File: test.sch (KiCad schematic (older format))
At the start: 6 parts, among them J1 Conn_01x32_Female, J2 Conn_01x32_Female, J3 DB9_Male, J4 Conn_01x32_Female, J5 Conn_01x32_Female, U1 MCP2551-I-SN

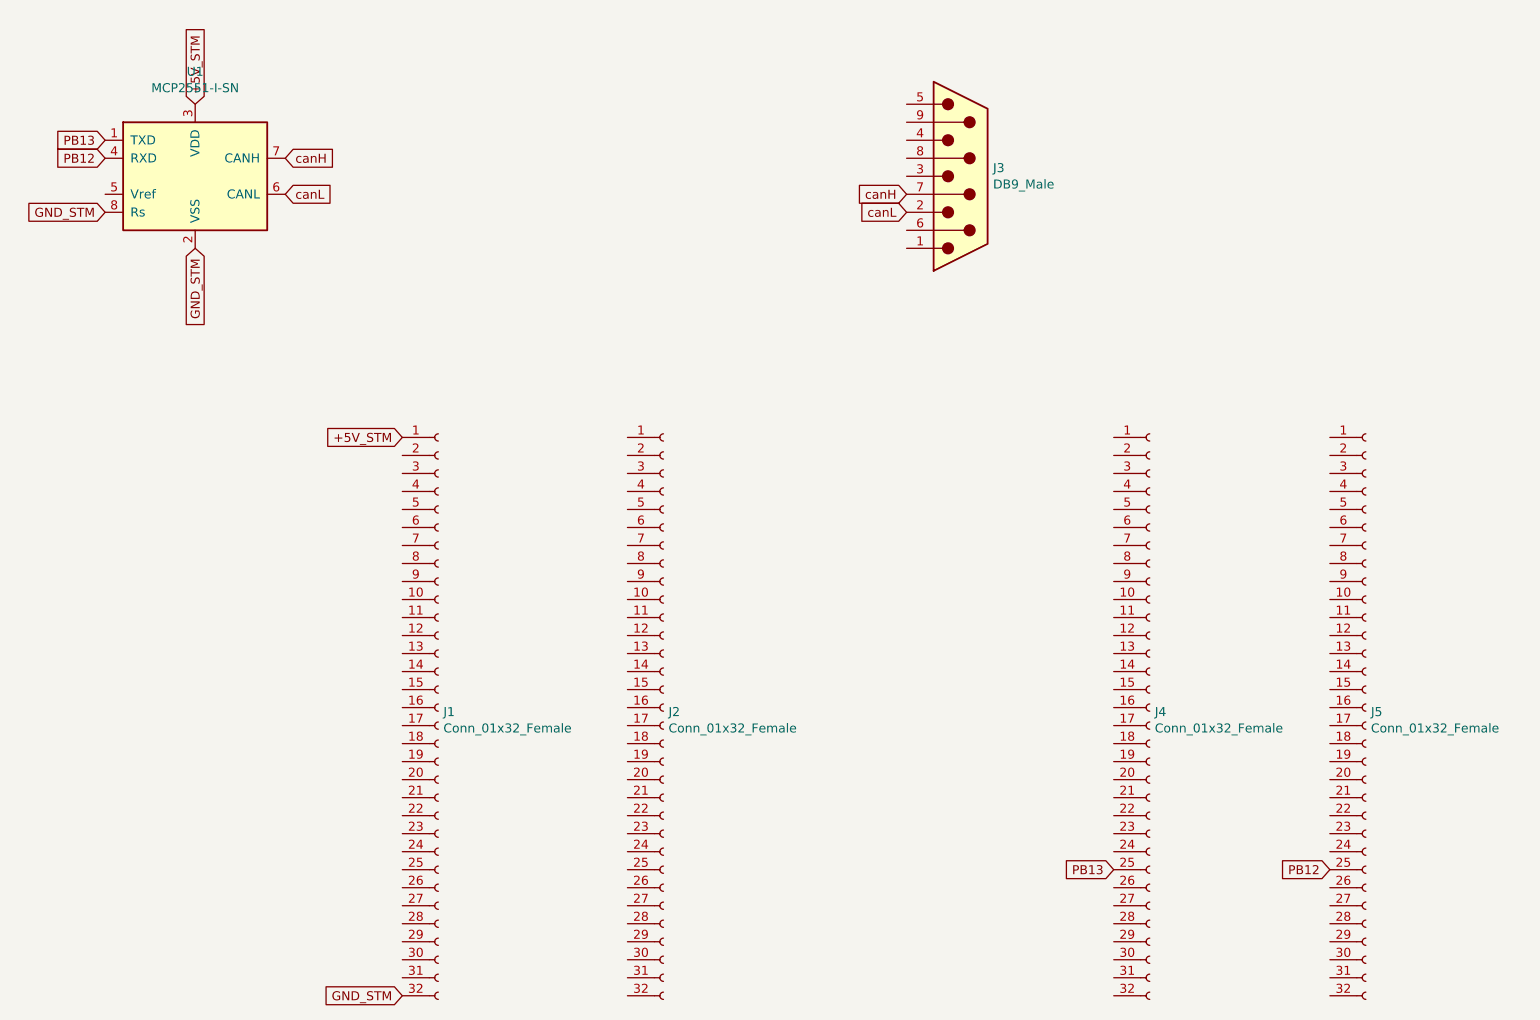
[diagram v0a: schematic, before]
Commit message: use less pin sockets
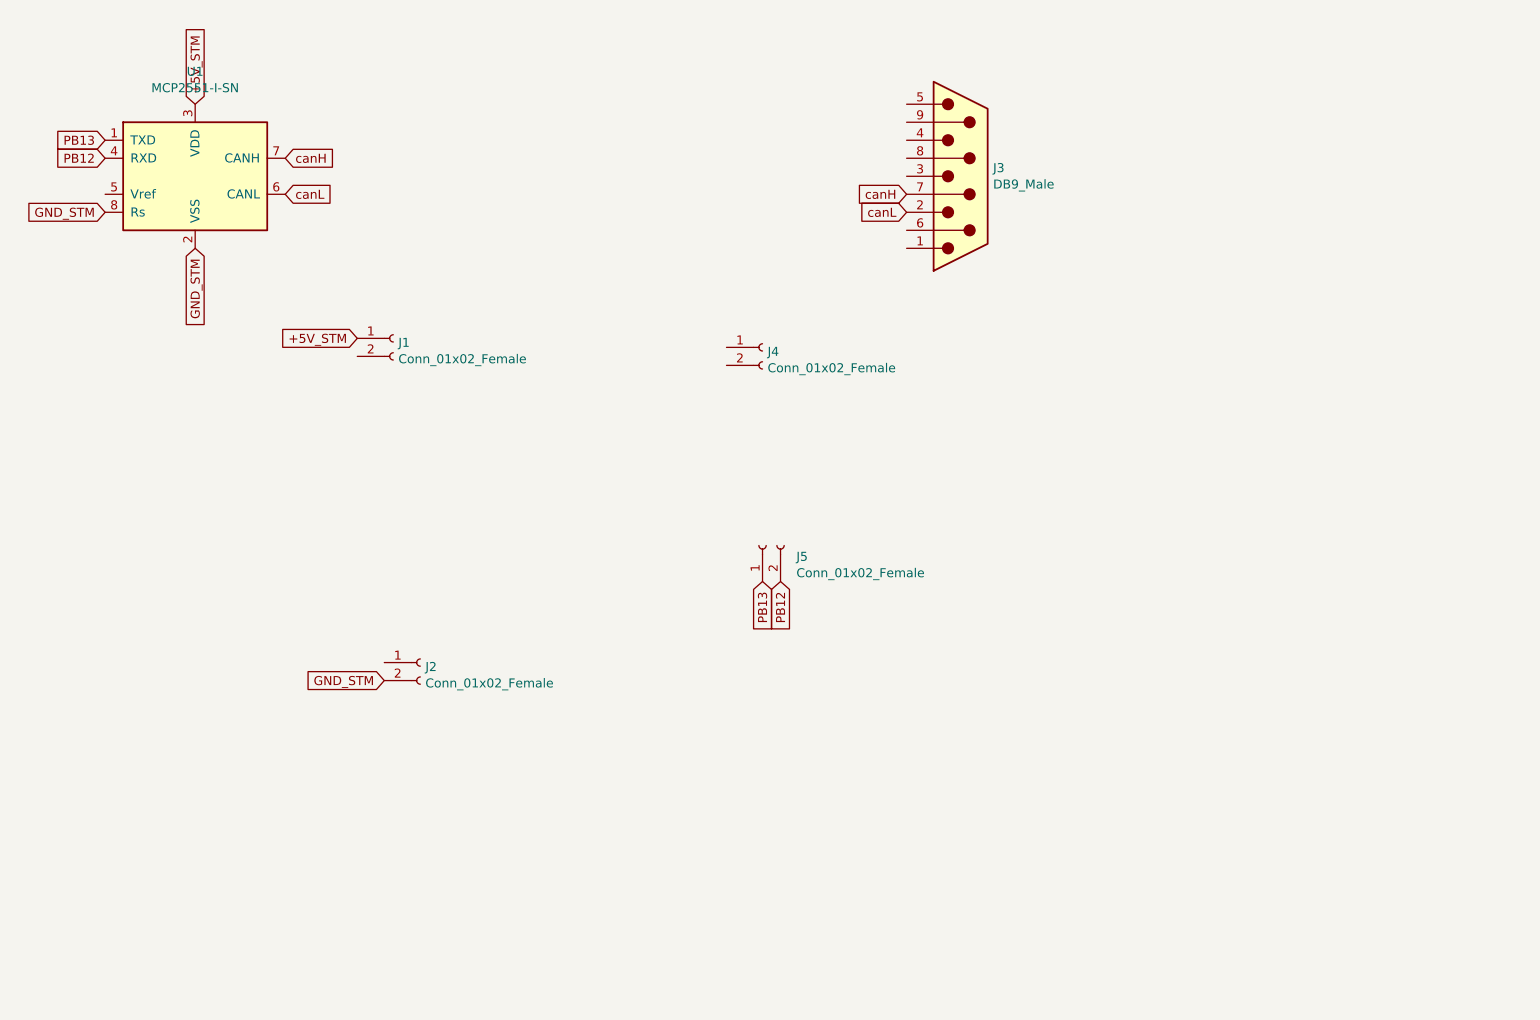
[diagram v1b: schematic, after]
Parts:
- removed J1, J2, J4, J5: Conn_01x32_Female, Connector_PinSocket_2.54mm:PinSocket_1x32_P2.54mm_Vertical, symbol Connector:Conn_01x32_Female
- added J1, J2, J4, J5: Conn_01x02_Female, Connector_PinSocket_2.54mm:PinSocket_1x02_P2.54mm_Vertical, symbol Connector:Conn_01x02_Female
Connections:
- net +5V_STM: now also J1.1 (Pin_1)
- net GND_STM: now also J2.2 (Pin_2)
- net PB12: now also J5.2 (Pin_2)
- net PB13: now also J5.1 (Pin_1)
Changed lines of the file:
@@
 Comment4 ""
 $EndDescr
-$Comp
-L Connector:Conn_01x32_Female J1
-U 1 1 5E3AAD21
-P 2950 4300
-F 0 "J1" H 2978 4276 50  0000 L CNN
-F 1 "Conn_01x32_Female" H 2978 4185 50  0000 L CNN
-F 2 "Connector_PinSocket_2.54mm:PinSocket_1x32_P2.54mm_Vertical" H 2950 4300 50  0001 C CNN
-F 3 "~" H 2950 4300 50  0001 C CNN
-	1    2950 4300
-	1    0    0    -1
-$EndComp
-$Comp
-L Connector:Conn_01x32_Female J2
-U 1 1 5E3AF919
-P 4200 4300
-F 0 "J2" H 4228 4276 50  0000 L CNN
-F 1 "Conn_01x32_Female" H 4228 4185 50  0000 L CNN
-F 2 "Connector_PinSocket_2.54mm:PinSocket_1x32_P2.54mm_Vertical" H 4200 4300 50  0001 C CNN
-F 3 "~" H 4200 4300 50  0001 C CNN
-	1    4200 4300
-	1    0    0    -1
-$EndComp
-$Comp
-L Connector:Conn_01x32_Female J4
-U 1 1 5E3B341A
-P 6900 4300
-F 0 "J4" H 6928 4276 50  0000 L CNN
-F 1 "Conn_01x32_Female" H 6928 4185 50  0000 L CNN
-F 2 "Connector_PinSocket_2.54mm:PinSocket_1x32_P2.54mm_Vertical" H 6900 4300 50  0001 C CNN
-F 3 "~" H 6900 4300 50  0001 C CNN
-	1    6900 4300
-	1    0    0    -1
-$EndComp
-$Comp
-L Connector:Conn_01x32_Female J5
-U 1 1 5E3B7068
-P 8100 4300
-F 0 "J5" H 8128 4276 50  0000 L CNN
-F 1 "Conn_01x32_Female" H 8128 4185 50  0000 L CNN
-F 2 "Connector_PinSocket_2.54mm:PinSocket_1x32_P2.54mm_Vertical" H 8100 4300 50  0001 C CNN
-F 3 "~" H 8100 4300 50  0001 C CNN
-	1    8100 4300
-	1    0    0    -1
-$EndComp
-Text GLabel 6700 5200 0    50   Input ~ 0
-PB13
-Text GLabel 7900 5200 0    50   Input ~ 0
+Text GLabel 4850 3600 3    50   Input ~ 0
 PB12
-Text GLabel 2750 2800 0    50   Input ~ 0
-+5V_STM
-Text GLabel 2750 5900 0    50   Input ~ 0
-GND_STM
 Text GLabel 1600 950  1    50   Input ~ 0
 +5V_STM
@@
 	1    0    0    -1
 $EndComp
+$Comp
+L Connector:Conn_01x02_Female J1
+U 1 1 5E4756EE
+P 2700 2250
+F 0 "J1" H 2728 2226 50  0000 L CNN
+F 1 "Conn_01x02_Female" H 2728 2135 50  0000 L CNN
+F 2 "Connector_PinSocket_2.54mm:PinSocket_1x02_P2.54mm_Vertical" H 2700 2250 50  0001 C CNN
+F 3 "~" H 2700 2250 50  0001 C CNN
+	1    2700 2250
+	1    0    0    -1
+$EndComp
+$Comp
+L Connector:Conn_01x02_Female J4
+U 1 1 5E48015E
+P 4750 2300
+F 0 "J4" H 4778 2276 50  0000 L CNN
+F 1 "Conn_01x02_Female" H 4778 2185 50  0000 L CNN
+F 2 "Connector_PinSocket_2.54mm:PinSocket_1x02_P2.54mm_Vertical" H 4750 2300 50  0001 C CNN
+F 3 "~" H 4750 2300 50  0001 C CNN
+	1    4750 2300
+	1    0    0    -1
+$EndComp
+$Comp
+L Connector:Conn_01x02_Female J2
+U 1 1 5E483C82
+P 2850 4050
+F 0 "J2" H 2878 4026 50  0000 L CNN
+F 1 "Conn_01x02_Female" H 2878 3935 50  0000 L CNN
+F 2 "Connector_PinSocket_2.54mm:PinSocket_1x02_P2.54mm_Vertical" H 2850 4050 50  0001 C CNN
+F 3 "~" H 2850 4050 50  0001 C CNN
+	1    2850 4050
+	1    0    0    -1
+$EndComp
+$Comp
+L Connector:Conn_01x02_Female J5
+U 1 1 5E48A586
+P 4750 3400
+F 0 "J5" V 4688 3212 50  0000 R CNN
+F 1 "Conn_01x02_Female" V 4597 3212 50  0000 R CNN
+F 2 "Connector_PinSocket_2.54mm:PinSocket_1x02_P2.54mm_Vertical" H 4750 3400 50  0001 C CNN
+F 3 "~" H 4750 3400 50  0001 C CNN
+	1    4750 3400
+	0    -1   -1   0
+$EndComp
+Text GLabel 2500 2250 0    50   Input ~ 0
++5V_STM
+Text GLabel 2650 4150 0    50   Input ~ 0
+GND_STM
+Text GLabel 4750 3600 3    50   Input ~ 0
+PB13
 $EndSCHEMATC

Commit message: Gerbers and BOM files
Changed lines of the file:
@@
 P 1600 1350
 F 0 "U1" H 1600 1931 50  0000 C CNN
-F 1 "MCP2551-I-SN" H 1600 1840 50  0000 C CNN
+F 1 "MCP2551-I-SN" H 1600 1350 50  0000 C CNN
 F 2 "Package_SO:SOIC-8_3.9x4.9mm_P1.27mm" H 1600 850 50  0001 C CIN
 F 3 "http://ww1.microchip.com/downloads/en/devicedoc/21667d.pdf" H 1600 1350 50  0001 C CNN

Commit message: housed db9
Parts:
- J3: footprint Connector_Dsub:DSUB-9_Male_Horizontal_P2.77x2.54mm_EdgePinOffset9.40mm -> Connector_Dsub:DSUB-9_Male_Horizontal_P2.77x2.84mm_EdgePinOffset4.94mm_Housed_MountingHolesOffset7.48mm
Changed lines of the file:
@@
 Text GLabel 2100 1450 2    50   Input ~ 0
 canL
-$Comp
-L Connector:DB9_Male J3
-U 1 1 5E492897
-P 5850 1350
-F 0 "J3" H 6030 1396 50  0000 L CNN
-F 1 "DB9_Male" H 6030 1305 50  0000 L CNN
-F 2 "Connector_Dsub:DSUB-9_Male_Horizontal_P2.77x2.54mm_EdgePinOffset9.40mm" H 5850 1350 50  0001 C CNN
-F 3 " ~" H 5850 1350 50  0001 C CNN
-	1    5850 1350
-	1    0    0    -1
-$EndComp
 Text GLabel 5550 1450 0    50   Input ~ 0
 canH
@@
 Text GLabel 4750 3600 3    50   Input ~ 0
 PB13
+$Comp
+L Connector:DB9_Male J3
+U 1 1 5E492897
+P 5850 1350
+F 0 "J3" H 6030 1396 50  0000 L CNN
+F 1 "DB9_Male" H 6030 1305 50  0000 L CNN
+F 2 "Connector_Dsub:DSUB-9_Male_Horizontal_P2.77x2.84mm_EdgePinOffset4.94mm_Housed_MountingHolesOffset7.48mm" H 5850 1350 50  0001 C CNN
+F 3 " ~" H 5850 1350 50  0001 C CNN
+	1    5850 1350
+	1    0    0    -1
+$EndComp
 $EndSCHEMATC

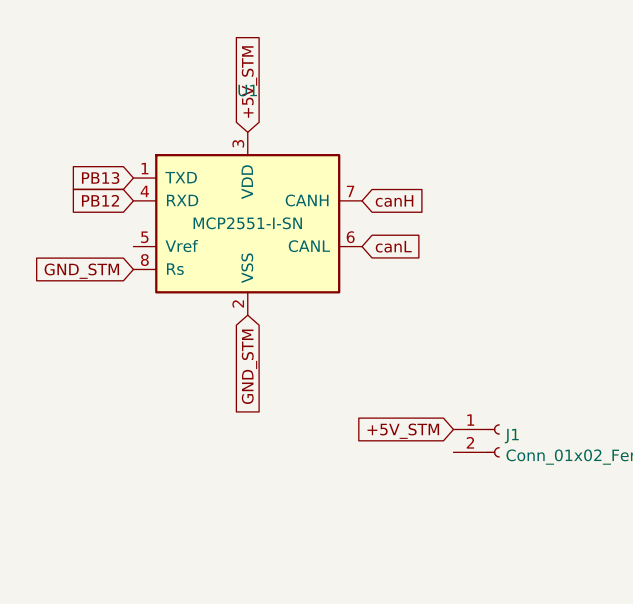
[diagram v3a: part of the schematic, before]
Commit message: regular mcp2551
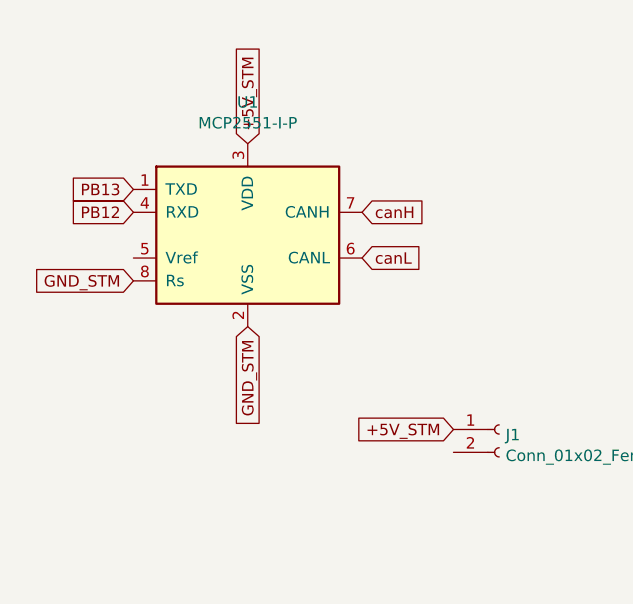
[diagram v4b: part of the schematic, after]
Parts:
- removed U1: MCP2551-I-SN, Package_SO:SOIC-8_3.9x4.9mm_P1.27mm, symbol Interface_CAN_LIN:MCP2551-I-SN
- added U1: MCP2551-I-P, Package_DIP:DIP-8_W7.62mm, symbol Interface_CAN_LIN:MCP2551-I-P
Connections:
- net +5V_STM: now also U1.3 (VDD)
- net GND_STM: now also U1.2 (VSS), U1.8 (Rs)
- net PB12: now also U1.4 (RXD)
- net PB13: now also U1.1 (TXD)
- net canH: now also U1.7 (CANH)
- net canL: now also U1.6 (CANL)
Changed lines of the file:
@@
 Text GLabel 4850 3600 3    50   Input ~ 0
 PB12
-Text GLabel 1600 950  1    50   Input ~ 0
+Text GLabel 1600 1000 1    50   Input ~ 0
 +5V_STM
-Text GLabel 1100 1250 0    50   Input ~ 0
+Text GLabel 1100 1300 0    50   Input ~ 0
 PB12
-Text GLabel 1100 1150 0    50   Input ~ 0
+Text GLabel 1100 1200 0    50   Input ~ 0
 PB13
-Text GLabel 1600 1750 3    50   Input ~ 0
+Text GLabel 1600 1800 3    50   Input ~ 0
 GND_STM
-Text GLabel 1100 1550 0    50   Input ~ 0
+Text GLabel 1100 1600 0    50   Input ~ 0
 GND_STM
-Text GLabel 2100 1250 2    50   Input ~ 0
+Text GLabel 2100 1300 2    50   Input ~ 0
 canH
-Text GLabel 2100 1450 2    50   Input ~ 0
+Text GLabel 2100 1500 2    50   Input ~ 0
 canL
 Text GLabel 5550 1450 0    50   Input ~ 0
@@
 Text GLabel 5550 1550 0    50   Input ~ 0
 canL
-$Comp
-L Interface_CAN_LIN:MCP2551-I-SN U1
-U 1 1 5E4B67C7
-P 1600 1350
-F 0 "U1" H 1600 1931 50  0000 C CNN
-F 1 "MCP2551-I-SN" H 1600 1350 50  0000 C CNN
-F 2 "Package_SO:SOIC-8_3.9x4.9mm_P1.27mm" H 1600 850 50  0001 C CIN
-F 3 "http://ww1.microchip.com/downloads/en/devicedoc/21667d.pdf" H 1600 1350 50  0001 C CNN
-	1    1600 1350
-	1    0    0    -1
-$EndComp
 $Comp
 L Connector:Conn_01x02_Female J1
@@
 	1    0    0    -1
 $EndComp
+$Comp
+L Interface_CAN_LIN:MCP2551-I-P U1
+U 1 1 5E503F33
+P 1600 1400
+F 0 "U1" H 1600 1981 50  0000 C CNN
+F 1 "MCP2551-I-P" H 1600 1890 50  0000 C CNN
+F 2 "Package_DIP:DIP-8_W7.62mm" H 1600 900 50  0001 C CIN
+F 3 "http://ww1.microchip.com/downloads/en/devicedoc/21667d.pdf" H 1600 1400 50  0001 C CNN
+	1    1600 1400
+	1    0    0    -1
+$EndComp
